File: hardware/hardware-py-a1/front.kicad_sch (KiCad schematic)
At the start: 28 parts, among them J3 LCD_socket, J4 Micro_SD_Card_Det2, J5 AudioJack4, Q8 BSS138, Q9 BSS138

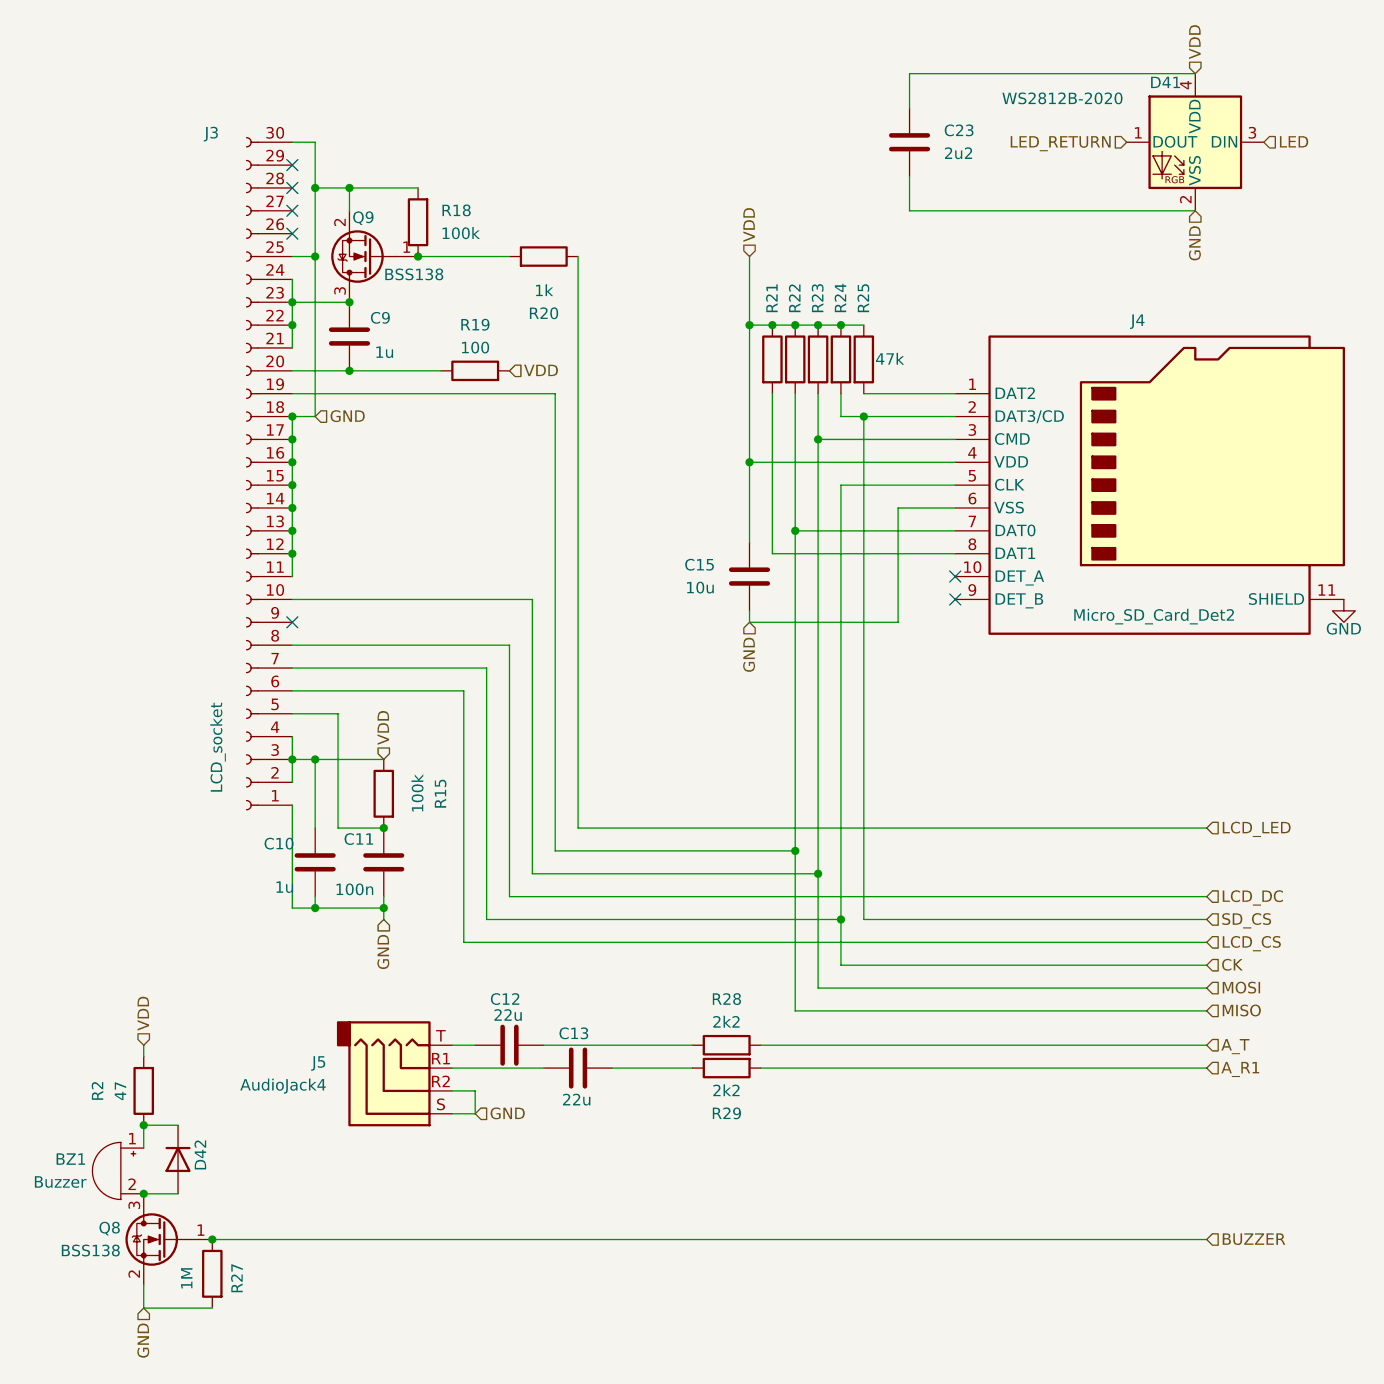
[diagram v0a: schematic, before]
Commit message: hw: passives values simpler, tantlum caps, silkscreen tweaks
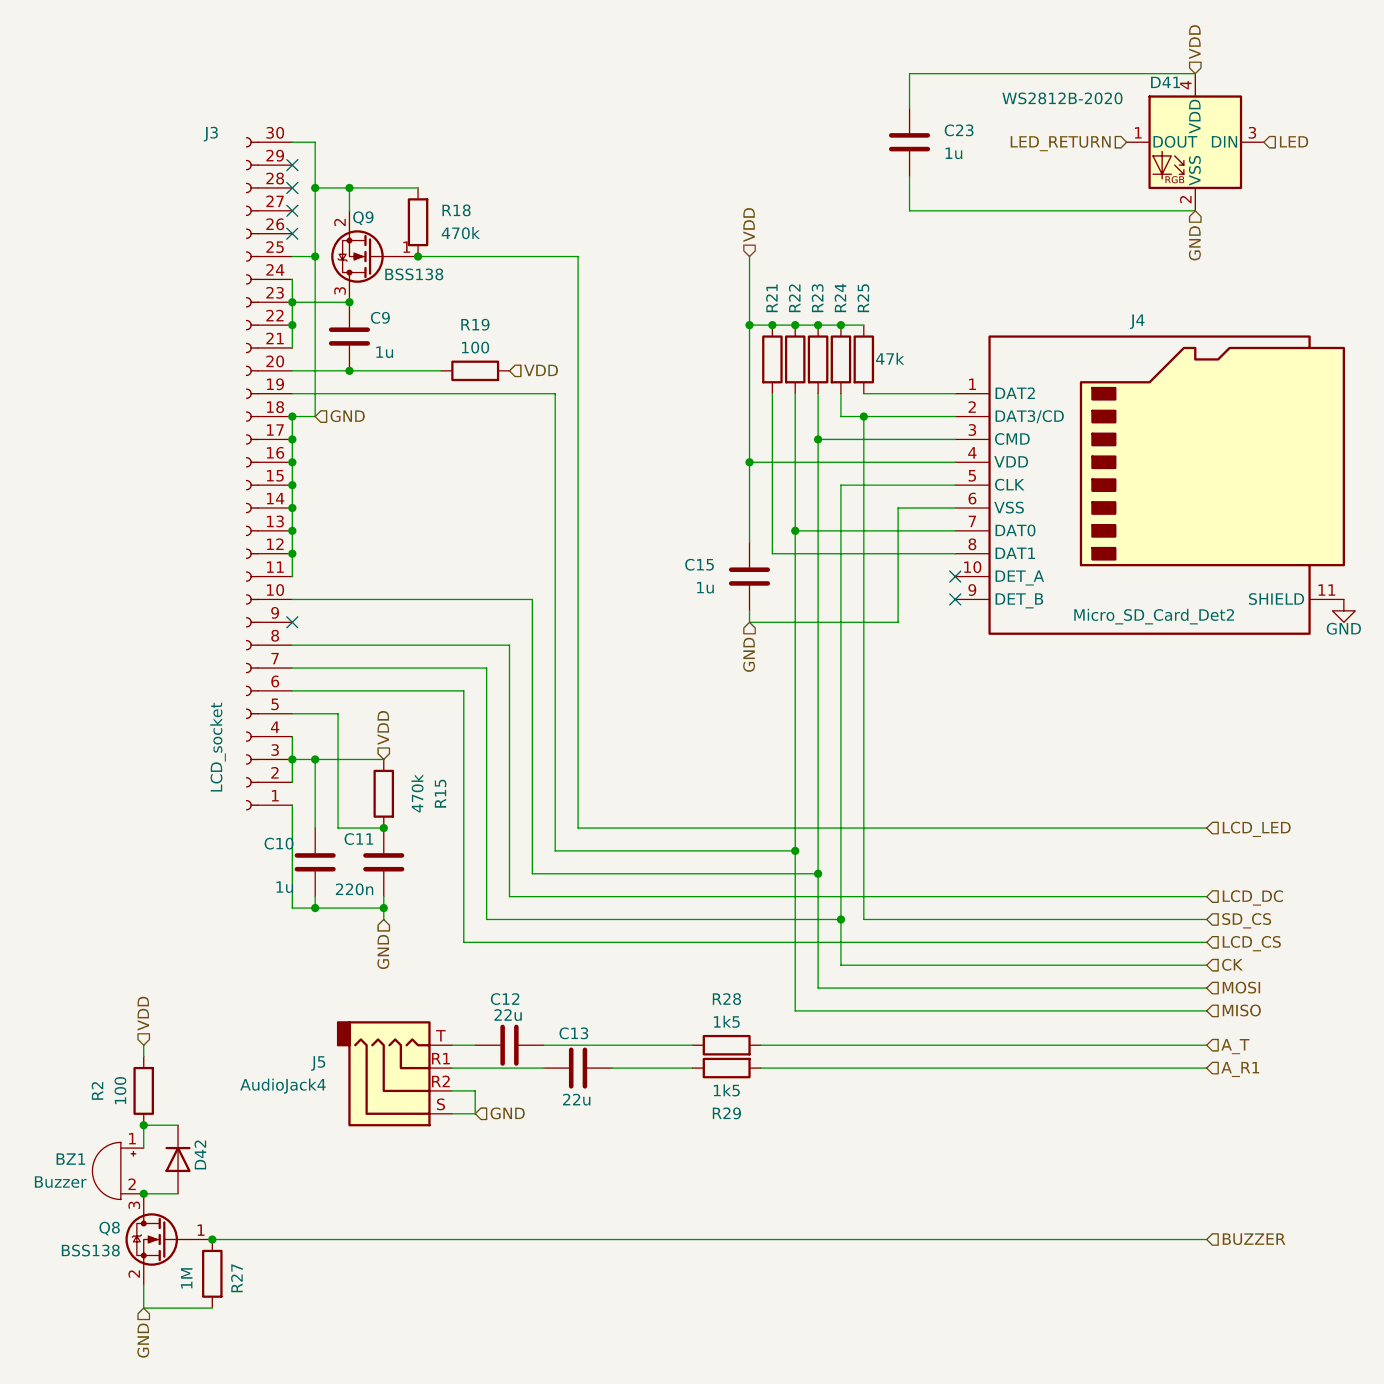
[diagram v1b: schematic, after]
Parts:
- removed R20: 1k, Resistor_SMD:R_0805_2012Metric_Pad1.20x1.40mm_HandSolder, symbol Device:R
- C10, C9: footprint Capacitor_SMD:C_0805_2012Metric -> Capacitor_SMD:C_0805_2012Metric_Pad1.18x1.45mm_HandSolder
- C11: value 100n -> 220n; footprint Capacitor_SMD:C_0805_2012Metric -> Capacitor_SMD:C_0805_2012Metric_Pad1.18x1.45mm_HandSolder
- C12, C13: footprint Capacitor_SMD:C_1210_3225Metric -> Capacitor_SMD:C_1206_3216Metric_Pad1.33x1.80mm_HandSolder
- C15: value 10u -> 1u; footprint Capacitor_SMD:C_0805_2012Metric -> Capacitor_SMD:C_0805_2012Metric_Pad1.18x1.45mm_HandSolder
- C23: value 2u2 -> 1u; footprint Capacitor_SMD:C_0805_2012Metric -> Capacitor_SMD:C_0805_2012Metric_Pad1.18x1.45mm_HandSolder
- D42: value D -> 1N4148
- R15, R18: value 100k -> 470k
- R2: value 47 -> 100
- R28, R29: value 2k2 -> 1k5
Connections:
- net LCD_LED: now also Q9.1 (G), R18.1
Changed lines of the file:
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@@
 	(wire
 		(pts
-			(xy 115.57 46.99) (xy 105.41 46.99)
+			(xy 105.41 46.99) (xy 123.19 46.99)
 		)
 		(stroke
@@
 			)
 		)
-		(property "Footprint" "Capacitor_SMD:C_0805_2012Metric"
+		(property "Footprint" "Capacitor_SMD:C_0805_2012Metric_Pad1.18x1.45mm_HandSolder"
 			(at 98.7552 59.69 0)
 			(effects
@@
 			)
 		)
-		(property "Value" "100k"
+		(property "Value" "470k"
 			(at 105.41 106.68 90)
 			(effects
@@
 			)
 		)
-		(property "Value" "2u2"
+		(property "Value" "1u"
 			(at 163.83 35.5599 0)
 			(effects
@@
 			)
 		)
-		(property "Footprint" "Capacitor_SMD:C_0805_2012Metric"
+		(property "Footprint" "Capacitor_SMD:C_0805_2012Metric_Pad1.18x1.45mm_HandSolder"
 			(at 160.9852 38.1 0)
 			(effects
@@
 	(symbol
 		(lib_id "Device:R")
-		(at 119.38 46.99 270)
-		(mirror x)
-		(unit 1)
-		(exclude_from_sim no)
-		(in_bom yes)
-		(on_board yes)
-		(dnp no)
-		(property "Reference" "R20"
-			(at 119.38 53.34 90)
-			(effects
-				(font
-					(size 1.27 1.27)
-				)
-			)
-		)
-		(property "Value" "1k"
-			(at 119.38 50.8 90)
-			(effects
-				(font
-					(size 1.27 1.27)
-				)
-			)
-		)
-		(property "Footprint" "Resistor_SMD:R_0805_2012Metric_Pad1.20x1.40mm_HandSolder"
-			(at 119.38 48.768 90)
-			(effects
-				(font
-					(size 1.27 1.27)
-				)
-				(hide yes)
-			)
-		)
-		(property "Datasheet" "~"
-			(at 119.38 46.99 0)
-			(effects
-				(font
-					(size 1.27 1.27)
-				)
-				(hide yes)
-			)
-		)
-		(property "Description" "Resistor"
-			(at 119.38 46.99 0)
-			(effects
-				(font
-					(size 1.27 1.27)
-				)
-				(hide yes)
-			)
-		)
-		(pin "1"
-		)
-		(pin "2"
-		)
-		(instances
-			(project "numcalcium"
-				(path "/842c0813-91d3-4f68-bc1f-ac3ce07be478/88d65574-4a55-44b9-b6d2-8e7d5a1c096b"
-					(reference "R20")
-					(unit 1)
-				)
-			)
-		)
-	)
-	(symbol
-		(lib_id "Device:R")
 		(at 152.4 58.42 0)
 		(unit 1)
@@
 			)
 		)
-		(property "Value" "D"
+		(property "Value" "1N4148"
 			(at 81.28 146.05 90)
 			(effects
@@
 			)
 		)
-		(property "Footprint" "Capacitor_SMD:C_1210_3225Metric"
+		(property "Footprint" "Capacitor_SMD:C_1206_3216Metric_Pad1.33x1.80mm_HandSolder"
 			(at 119.38 135.5852 0)
 			(effects
@@
 			)
 		)
-		(property "Footprint" "Capacitor_SMD:C_1210_3225Metric"
+		(property "Footprint" "Capacitor_SMD:C_1206_3216Metric_Pad1.33x1.80mm_HandSolder"
 			(at 127 138.1252 0)
 			(effects
@@
 			)
 		)
-		(property "Value" "10u"
+		(property "Value" "1u"
 			(at 138.43 83.8199 0)
 			(effects
@@
 			)
 		)
-		(property "Footprint" "Capacitor_SMD:C_0805_2012Metric"
+		(property "Footprint" "Capacitor_SMD:C_0805_2012Metric_Pad1.18x1.45mm_HandSolder"
 			(at 141.2748 86.36 0)
 			(effects
@@
 			)
 		)
-		(property "Value" "2k2"
+		(property "Value" "1k5"
 			(at 139.7 132.08 90)
 			(effects
@@
 			)
 		)
-		(property "Value" "100n"
+		(property "Value" "220n"
 			(at 100.584 117.348 0)
 			(effects
@@
 			)
 		)
-		(property "Footprint" "Capacitor_SMD:C_0805_2012Metric"
+		(property "Footprint" "Capacitor_SMD:C_0805_2012Metric_Pad1.18x1.45mm_HandSolder"
 			(at 100.6348 118.11 0)
 			(effects
@@
 			)
 		)
-		(property "Value" "100k"
+		(property "Value" "470k"
 			(at 107.95 44.4499 0)
 			(effects
@@
 			)
 		)
-		(property "Value" "2k2"
+		(property "Value" "1k5"
 			(at 139.7 139.7 90)
 			(effects
@@
 			)
 		)
-		(property "Value" "47"
+		(property "Value" "100"
 			(at 72.39 139.7 90)
 			(effects
@@
 			)
 		)
-		(property "Footprint" "Capacitor_SMD:C_0805_2012Metric"
+		(property "Footprint" "Capacitor_SMD:C_0805_2012Metric_Pad1.18x1.45mm_HandSolder"
 			(at 93.0148 118.11 0)
 			(effects
